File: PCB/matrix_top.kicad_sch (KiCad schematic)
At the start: 56 parts, among them J21 Conn_02x02_Top_Bottom, J22 Conn_02x02_Top_Bottom, J23 Conn_02x02_Top_Bottom, J24 Conn_02x02_Top_Bottom, J27 Conn_02x02_Top_Bottom, J28 Conn_02x02_Top_Bottom

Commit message: 部品仮配置
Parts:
- J23: renamed from J21; footprint Connector_PinHeader_2.00mm:PinHeader_2x02_P2.00mm_Vertical -> locallib:PinHeader_2x02_P2.00mm_Vertical_Centered
- J24: renamed from J22; footprint Connector_PinHeader_2.00mm:PinHeader_2x02_P2.00mm_Vertical -> locallib:PinHeader_2x02_P2.00mm_Vertical_Centered
- J25: renamed from J23; footprint Connector_PinHeader_2.00mm:PinHeader_2x02_P2.00mm_Vertical -> locallib:PinHeader_2x02_P2.00mm_Vertical_Centered
- J26: renamed from J24; footprint Connector_PinHeader_2.00mm:PinHeader_2x02_P2.00mm_Vertical -> locallib:PinHeader_2x02_P2.00mm_Vertical_Centered
- J27, J28: footprint Connector_PinHeader_2.00mm:PinHeader_2x02_P2.00mm_Vertical -> locallib:PinHeader_2x02_P2.00mm_Vertical_Centered
- renumbered EXT_C16 to EXT_TC0, EXT_C17 to EXT_TC1, EXT_C18 to EXT_TC2, EXT_C19 to EXT_TC3, EXT_C20 to EXT_TC4, EXT_C21 to EXT_TC5, EXT_C22 to EXT_TC6, EXT_C23 to EXT_TC7, EXT_R20 to EXT_TR0, EXT_R22 to EXT_TR1, EXT_R21 to EXT_TR5, EXT_R23 to EXT_TR6
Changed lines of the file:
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@@
   (symbol (lib_id "Connector_Generic:Conn_02x02_Odd_Even") (at 90.805 132.08 0) (unit 1)
     (in_bom yes) (on_board yes) (fields_autoplaced)
-    (property "Reference" "J22" (id 0) (at 92.075 127.1102 0))
+    (property "Reference" "J24" (id 0) (at 92.075 127.1102 0))
     (property "Value" "Conn_02x02_Top_Bottom" (id 1) (at 92.075 129.6471 0))
-    (property "Footprint" "Connector_PinHeader_2.00mm:PinHeader_2x02_P2.00mm_Vertical" (id 2) (at 90.805 132.08 0)
+    (property "Footprint" "locallib:PinHeader_2x02_P2.00mm_Vertical_Centered" (id 2) (at 90.805 132.08 0)
       (effects (font (size 1.27 1.27)) hide)
     )
@@
   (symbol (lib_id "Connector_Generic:Conn_01x01") (at 284.48 101.6 0) (unit 1)
     (in_bom yes) (on_board yes)
-    (property "Reference" "EXT_R23" (id 0) (at 286.512 100.5332 0)
+    (property "Reference" "EXT_TR6" (id 0) (at 286.512 100.5332 0)
       (effects (font (size 1.27 1.27)) (justify left))
     )
@@
   (symbol (lib_id "Connector_Generic:Conn_01x01") (at 170.18 110.49 270) (unit 1)
     (in_bom yes) (on_board yes)
-    (property "Reference" "EXT_C20" (id 0) (at 172.212 107.2388 90)
+    (property "Reference" "EXT_TC4" (id 0) (at 172.212 107.2388 90)
       (effects (font (size 1.27 1.27)) (justify left))
     )
@@
   (symbol (lib_id "Connector_Generic:Conn_01x01") (at 137.16 110.49 270) (unit 1)
     (in_bom yes) (on_board yes)
-    (property "Reference" "EXT_C19" (id 0) (at 139.192 107.2388 90)
+    (property "Reference" "EXT_TC3" (id 0) (at 139.192 107.2388 90)
       (effects (font (size 1.27 1.27)) (justify left))
     )
@@
   (symbol (lib_id "Connector_Generic:Conn_01x01") (at 203.2 110.49 270) (unit 1)
     (in_bom yes) (on_board yes)
-    (property "Reference" "EXT_C21" (id 0) (at 205.232 107.2388 90)
+    (property "Reference" "EXT_TC5" (id 0) (at 205.232 107.2388 90)
       (effects (font (size 1.27 1.27)) (justify left))
     )
@@
     (property "Reference" "J27" (id 0) (at 92.075 141.0802 0))
     (property "Value" "Conn_02x02_Top_Bottom" (id 1) (at 92.075 143.6171 0))
-    (property "Footprint" "Connector_PinHeader_2.00mm:PinHeader_2x02_P2.00mm_Vertical" (id 2) (at 90.805 146.05 0)
+    (property "Footprint" "locallib:PinHeader_2x02_P2.00mm_Vertical_Centered" (id 2) (at 90.805 146.05 0)
       (effects (font (size 1.27 1.27)) hide)
     )
@@
     (property "Reference" "J28" (id 0) (at 142.875 141.0802 0))
     (property "Value" "Conn_02x02_Top_Bottom" (id 1) (at 142.875 143.6171 0))
-    (property "Footprint" "Connector_PinHeader_2.00mm:PinHeader_2x02_P2.00mm_Vertical" (id 2) (at 141.605 146.05 0)
+    (property "Footprint" "locallib:PinHeader_2x02_P2.00mm_Vertical_Centered" (id 2) (at 141.605 146.05 0)
       (effects (font (size 1.27 1.27)) hide)
     )
@@
   (symbol (lib_id "Connector_Generic:Conn_02x02_Odd_Even") (at 40.005 132.08 0) (unit 1)
     (in_bom yes) (on_board yes) (fields_autoplaced)
-    (property "Reference" "J21" (id 0) (at 41.275 127.1102 0))
+    (property "Reference" "J23" (id 0) (at 41.275 127.1102 0))
     (property "Value" "Conn_02x02_Top_Bottom" (id 1) (at 41.275 129.6471 0))
-    (property "Footprint" "Connector_PinHeader_2.00mm:PinHeader_2x02_P2.00mm_Vertical" (id 2) (at 40.005 132.08 0)
+    (property "Footprint" "locallib:PinHeader_2x02_P2.00mm_Vertical_Centered" (id 2) (at 40.005 132.08 0)
       (effects (font (size 1.27 1.27)) hide)
     )
@@
   (symbol (lib_id "Connector_Generic:Conn_01x01") (at 236.22 110.49 270) (unit 1)
     (in_bom yes) (on_board yes)
-    (property "Reference" "EXT_C22" (id 0) (at 238.252 107.2388 90)
+    (property "Reference" "EXT_TC6" (id 0) (at 238.252 107.2388 90)
       (effects (font (size 1.27 1.27)) (justify left))
     )
@@
   (symbol (lib_id "Connector_Generic:Conn_01x01") (at 269.24 110.49 270) (unit 1)
     (in_bom yes) (on_board yes)
-    (property "Reference" "EXT_C23" (id 0) (at 271.272 107.2388 90)
+    (property "Reference" "EXT_TC7" (id 0) (at 271.272 107.2388 90)
       (effects (font (size 1.27 1.27)) (justify left))
     )
@@
   (symbol (lib_id "Connector_Generic:Conn_02x02_Odd_Even") (at 192.405 132.08 0) (unit 1)
     (in_bom yes) (on_board yes) (fields_autoplaced)
-    (property "Reference" "J24" (id 0) (at 193.675 127.1102 0))
+    (property "Reference" "J26" (id 0) (at 193.675 127.1102 0))
     (property "Value" "Conn_02x02_Top_Bottom" (id 1) (at 193.675 129.6471 0))
-    (property "Footprint" "Connector_PinHeader_2.00mm:PinHeader_2x02_P2.00mm_Vertical" (id 2) (at 192.405 132.08 0)
+    (property "Footprint" "locallib:PinHeader_2x02_P2.00mm_Vertical_Centered" (id 2) (at 192.405 132.08 0)
       (effects (font (size 1.27 1.27)) hide)
     )
@@
   (symbol (lib_id "Connector_Generic:Conn_01x01") (at 284.48 99.06 0) (unit 1)
     (in_bom yes) (on_board yes)
-    (property "Reference" "EXT_R22" (id 0) (at 286.512 97.9932 0)
+    (property "Reference" "EXT_TR1" (id 0) (at 286.512 97.9932 0)
       (effects (font (size 1.27 1.27)) (justify left))
     )
@@
   (symbol (lib_id "Connector_Generic:Conn_01x01") (at 104.14 110.49 270) (unit 1)
     (in_bom yes) (on_board yes)
-    (property "Reference" "EXT_C18" (id 0) (at 106.172 107.2388 90)
+    (property "Reference" "EXT_TC2" (id 0) (at 106.172 107.2388 90)
       (effects (font (size 1.27 1.27)) (justify left))
     )
@@
   (symbol (lib_id "Connector_Generic:Conn_01x01") (at 284.48 67.31 0) (unit 1)
     (in_bom yes) (on_board yes)
-    (property "Reference" "EXT_R20" (id 0) (at 286.512 66.2432 0)
+    (property "Reference" "EXT_TR0" (id 0) (at 286.512 66.2432 0)
       (effects (font (size 1.27 1.27)) (justify left))
     )
@@
   (symbol (lib_id "Connector_Generic:Conn_01x01") (at 284.48 69.85 0) (unit 1)
     (in_bom yes) (on_board yes)
-    (property "Reference" "EXT_R21" (id 0) (at 286.512 68.7832 0)
+    (property "Reference" "EXT_TR5" (id 0) (at 286.512 68.7832 0)
       (effects (font (size 1.27 1.27)) (justify left))
     )
@@
   (symbol (lib_id "Connector_Generic:Conn_02x02_Odd_Even") (at 141.605 132.08 0) (unit 1)
     (in_bom yes) (on_board yes) (fields_autoplaced)
-    (property "Reference" "J23" (id 0) (at 142.875 127.1102 0))
+    (property "Reference" "J25" (id 0) (at 142.875 127.1102 0))
     (property "Value" "Conn_02x02_Top_Bottom" (id 1) (at 142.875 129.6471 0))
-    (property "Footprint" "Connector_PinHeader_2.00mm:PinHeader_2x02_P2.00mm_Vertical" (id 2) (at 141.605 132.08 0)
+    (property "Footprint" "locallib:PinHeader_2x02_P2.00mm_Vertical_Centered" (id 2) (at 141.605 132.08 0)
       (effects (font (size 1.27 1.27)) hide)
     )
@@
   (symbol (lib_id "Connector_Generic:Conn_01x01") (at 38.1 110.49 270) (unit 1)
     (in_bom yes) (on_board yes)
-    (property "Reference" "EXT_C16" (id 0) (at 40.132 107.2388 90)
+    (property "Reference" "EXT_TC0" (id 0) (at 40.132 107.2388 90)
       (effects (font (size 1.27 1.27)) (justify left))
     )
@@
   (symbol (lib_id "Connector_Generic:Conn_01x01") (at 71.12 110.49 270) (unit 1)
     (in_bom yes) (on_board yes)
-    (property "Reference" "EXT_C17" (id 0) (at 73.152 107.2388 90)
-      (effects (font (size 1.27 1.27)) (justify left))
-    )
+    (property "Reference" "EXT_TC1" (id 0) (at 73.152 107.2388 90)
+      (effects (font (size 1.27 1.27)) (justify left))
+    )

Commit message: JSTコネクタとスペーサーでなんとするテスト
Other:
- note added: "Mid to Top: require 12 pins"
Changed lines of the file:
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@@
     (effects (font (size 2.54 2.54) (thickness 0.508) bold) (justify left bottom))
+  )
+  (text "Mid to Top: require 12 pins" (at 179.07 151.13 0)
+    (effects (font (size 5.08 5.08) (thickness 1.016) bold) (justify left bottom))
   )
   (text "Top plate" (at 13.97 17.78 0)

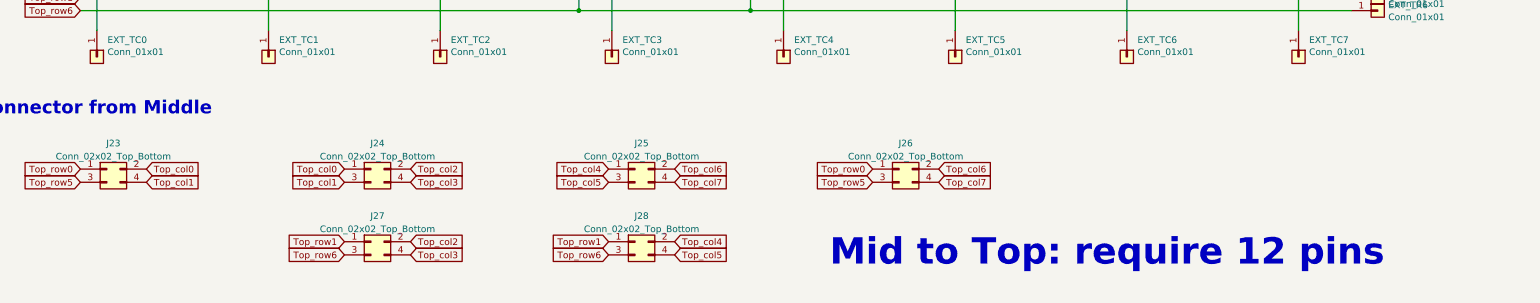
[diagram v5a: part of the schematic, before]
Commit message: JSTコネクタとスペーサーに置き換え
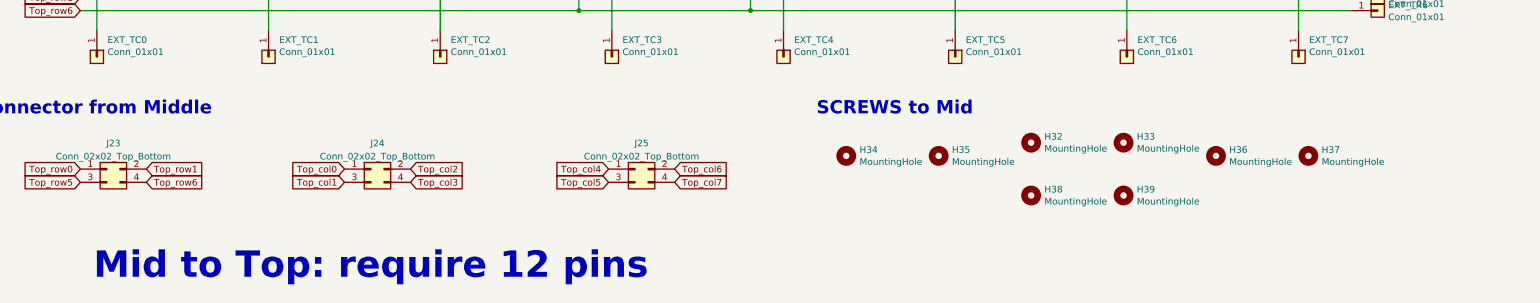
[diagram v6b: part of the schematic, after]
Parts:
- removed J26, J27, J28: Conn_02x02_Top_Bottom, locallib:PinHeader_2x02_P2.00mm_Vertical_Centered, symbol Connector_Generic:Conn_02x02_Odd_Even
- added H32, H33, H34, H35, H36, H37, H38, H39: MountingHole, MountingHole:MountingHole_2.2mm_M2_No_Cu, symbol Mechanical:MountingHole
- J23, J24, J25: footprint locallib:PinHeader_2x02_P2.00mm_Vertical_Centered -> Connector_JST:JST_SH_SM04B-SRSS-TB_1x04-1MP_P1.00mm_Horizontal
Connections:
- net Top_col0: no longer J23.2 (Pin_2)
- net Top_col1: no longer J23.4 (Pin_4)
- net Top_row1: now also J23.2 (Pin_2)
- net Top_row6: now also J23.4 (Pin_4)
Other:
- note added: "SCREWS to Mid"

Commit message: コネクタ位置考え中
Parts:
- added J30, J31, J32: Conn_01x04, Connector_PinHeader_2.54mm:PinHeader_1x04_P2.54mm_Vertical, symbol Connector_Generic:Conn_01x04
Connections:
- net Top_col0: now also J31.1 (Pin_1)
- net Top_col1: now also J31.3 (Pin_3)
- net Top_col2: now also J31.2 (Pin_2)
- net Top_col3: now also J31.4 (Pin_4)
- net Top_col4: now also J32.1 (Pin_1)
- net Top_col5: now also J32.3 (Pin_3)
- net Top_col6: now also J32.2 (Pin_2)
- net Top_col7: now also J32.4 (Pin_4)
- net Top_row0: now also J30.1 (Pin_1)
- net Top_row1: now also J30.2 (Pin_2)
- net Top_row5: now also J30.3 (Pin_3)
- net Top_row6: now also J30.4 (Pin_4)
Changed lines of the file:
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@@
+    (stroke (width 0) (type default) (color 0 0 0 0))
+  )
+  (wire (pts (xy 34.925 134.62) (xy 41.275 154.305))
     (stroke (width 0) (type default) (color 0 0 0 0))
   )
@@
     (stroke (width 0) (type default) (color 0 0 0 0))
   )
+  (wire (pts (xy 149.225 134.62) (xy 142.875 156.845))
+    (stroke (width 0) (type default) (color 0 0 0 0))
+  )
   (wire (pts (xy 71.12 58.42) (xy 71.12 105.41))
     (stroke (width 0) (type default) (color 0 0 0 0))
@@
     (stroke (width 0) (type default) (color 0 0 0 0))
   )
+  (wire (pts (xy 92.075 149.225) (xy 85.725 132.08))
+    (stroke (width 0) (type default) (color 0 0 0 0))
+  )
   (wire (pts (xy 153.67 46.99) (xy 137.16 46.99))
     (stroke (width 0) (type default) (color 0 0 0 0))
@@
     (stroke (width 0) (type default) (color 0 0 0 0))
   )
+  (wire (pts (xy 98.425 132.08) (xy 92.075 151.765))
+    (stroke (width 0) (type default) (color 0 0 0 0))
+  )
   (wire (pts (xy 38.1 46.99) (xy 38.1 58.42))
     (stroke (width 0) (type default) (color 0 0 0 0))
@@
     (stroke (width 0) (type default) (color 0 0 0 0))
   )
+  (wire (pts (xy 47.625 132.08) (xy 41.275 151.765))
+    (stroke (width 0) (type default) (color 0 0 0 0))
+  )
   (wire (pts (xy 163.83 97.79) (xy 163.83 101.6))
     (stroke (width 0) (type default) (color 0 0 0 0))
@@
     (stroke (width 0) (type default) (color 0 0 0 0))
   )
+  (wire (pts (xy 41.275 149.225) (xy 34.925 132.08))
+    (stroke (width 0) (type default) (color 0 0 0 0))
+  )
+  (wire (pts (xy 136.525 134.62) (xy 142.875 154.305))
+    (stroke (width 0) (type default) (color 0 0 0 0))
+  )
   (wire (pts (xy 97.79 66.04) (xy 97.79 69.85))
     (stroke (width 0) (type default) (color 0 0 0 0))
@@
     (stroke (width 0) (type default) (color 0 0 0 0))
   )
+  (wire (pts (xy 41.275 156.845) (xy 47.625 134.62))
+    (stroke (width 0) (type default) (color 0 0 0 0))
+  )
   (wire (pts (xy 114.3 66.04) (xy 114.3 67.31))
     (stroke (width 0) (type default) (color 0 0 0 0))
@@
     (stroke (width 0) (type default) (color 0 0 0 0))
   )
+  (wire (pts (xy 92.075 154.305) (xy 85.725 134.62))
+    (stroke (width 0) (type default) (color 0 0 0 0))
+  )
   (wire (pts (xy 252.73 46.99) (xy 252.73 58.42))
     (stroke (width 0) (type default) (color 0 0 0 0))
@@
     (stroke (width 0) (type default) (color 0 0 0 0))
   )
+  (wire (pts (xy 98.425 134.62) (xy 92.075 156.845))
+    (stroke (width 0) (type default) (color 0 0 0 0))
+  )
   (wire (pts (xy 34.925 99.06) (xy 147.32 99.06))
     (stroke (width 0) (type default) (color 0 0 0 0))
@@
     (stroke (width 0) (type default) (color 0 0 0 0))
   )
+  (wire (pts (xy 142.875 151.765) (xy 149.225 132.08))
+    (stroke (width 0) (type default) (color 0 0 0 0))
+  )
   (wire (pts (xy 48.26 66.04) (xy 48.26 67.31))
     (stroke (width 0) (type default) (color 0 0 0 0))
@@
   )
   (wire (pts (xy 34.925 101.6) (xy 130.81 101.6))
+    (stroke (width 0) (type default) (color 0 0 0 0))
+  )
+  (wire (pts (xy 136.525 132.08) (xy 142.875 149.225))
     (stroke (width 0) (type default) (color 0 0 0 0))
   )
@@
     (effects (font (size 2.54 2.54) (thickness 0.508) bold) (justify left bottom))
   )
-  (text "Mid to Top: require 12 pins" (at 37.465 153.67 0)
+  (text "Mid to Top: require 12 pins" (at 24.765 190.5 0)
     (effects (font (size 5.08 5.08) (thickness 1.016) bold) (justify left bottom))
   )
@@
     )
   )
+  (symbol (lib_id "Connector_Generic:Conn_01x04") (at 137.795 151.765 0) (mirror y) (unit 1)
+    (in_bom yes) (on_board yes) (fields_autoplaced)
+    (property "Reference" "J32" (id 0) (at 137.795 144.2552 0))
+    (property "Value" "Conn_01x04" (id 1) (at 137.795 146.7921 0))
+    (property "Footprint" "Connector_PinHeader_2.54mm:PinHeader_1x04_P2.54mm_Vertical" (id 2) (at 137.795 151.765 0)
+      (effects (font (size 1.27 1.27)) hide)
+    )
+    (property "Datasheet" "~" (id 3) (at 137.795 151.765 0)
+      (effects (font (size 1.27 1.27)) hide)
+    )
+    (pin "1")
+    (pin "2")
+    (pin "3")
+    (pin "4")
+  )
   (symbol (lib_id "Connector_Generic:Conn_01x01") (at 170.18 110.49 270) (unit 1)
     (in_bom yes) (on_board yes)
@@
     (pin "2")
   )
+  (symbol (lib_id "Connector_Generic:Conn_01x04") (at 86.995 151.765 0) (mirror y) (unit 1)
+    (in_bom yes) (on_board yes) (fields_autoplaced)
+    (property "Reference" "J31" (id 0) (at 86.995 144.2552 0))
+    (property "Value" "Conn_01x04" (id 1) (at 86.995 146.7921 0))
+    (property "Footprint" "Connector_PinHeader_2.54mm:PinHeader_1x04_P2.54mm_Vertical" (id 2) (at 86.995 151.765 0)
+      (effects (font (size 1.27 1.27)) hide)
+    )
+    (property "Datasheet" "~" (id 3) (at 86.995 151.765 0)
+      (effects (font (size 1.27 1.27)) hide)
+    )
+    (pin "1")
+    (pin "2")
+    (pin "3")
+    (pin "4")
+  )
   (symbol (lib_id "Connector_Generic:Conn_01x01") (at 137.16 110.49 270) (unit 1)
     (in_bom yes) (on_board yes)
@@
     (pin "2")
   )
+  (symbol (lib_id "Connector_Generic:Conn_01x04") (at 36.195 151.765 0) (mirror y) (unit 1)
+    (in_bom yes) (on_board yes) (fields_autoplaced)
+    (property "Reference" "J30" (id 0) (at 36.195 144.2552 0))
+    (property "Value" "Conn_01x04" (id 1) (at 36.195 146.7921 0))
+    (property "Footprint" "Connector_PinHeader_2.54mm:PinHeader_1x04_P2.54mm_Vertical" (id 2) (at 36.195 151.765 0)
+      (effects (font (size 1.27 1.27)) hide)
+    )
+    (property "Datasheet" "~" (id 3) (at 36.195 151.765 0)
+      (effects (font (size 1.27 1.27)) hide)
+    )
+    (pin "1")
+    (pin "2")
+    (pin "3")
+    (pin "4")
+  )
   (symbol (lib_id "Switch:SW_Push") (at 125.73 90.17 0) (unit 1)
